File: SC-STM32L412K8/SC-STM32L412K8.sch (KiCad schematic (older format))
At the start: 72 parts, among them J1 usb, J10 PWM, J11 Vibro, J12 +3v, J13 +vibro, J2 +29.6 SiPM, J3 TxD, J4 RxD, J5 SWDIO, J6 SWCLK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

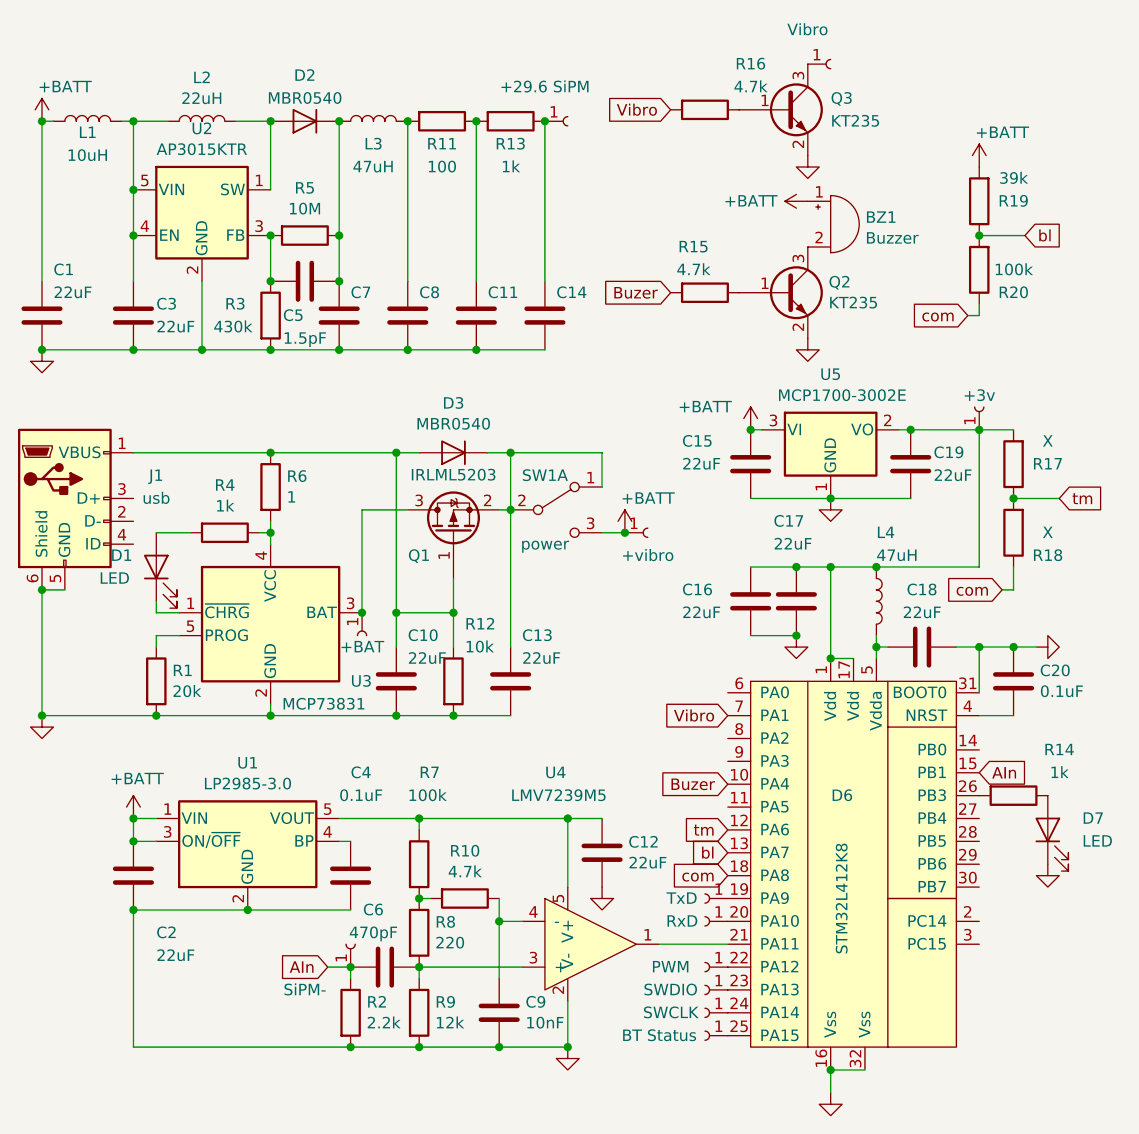
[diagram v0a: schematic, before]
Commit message: изменено:      SC-STM32L412K8/SC-STM32L412K8.kicad_pcb 	изменено:      SC-STM32L412K8/SC-STM32L412K8.kicad_pcb-bak 	изменено:      SC-STM32L412K8/SC-STM32L412K8.net 	изменено:      SC-STM32L412K8/SC-STM32L412K8.sch 	изменено:      SC-STM32L412K8/SC-STM32L412K8.sch-bak 	изменено:      STM32L412K8code/.settings/language.settings.xml
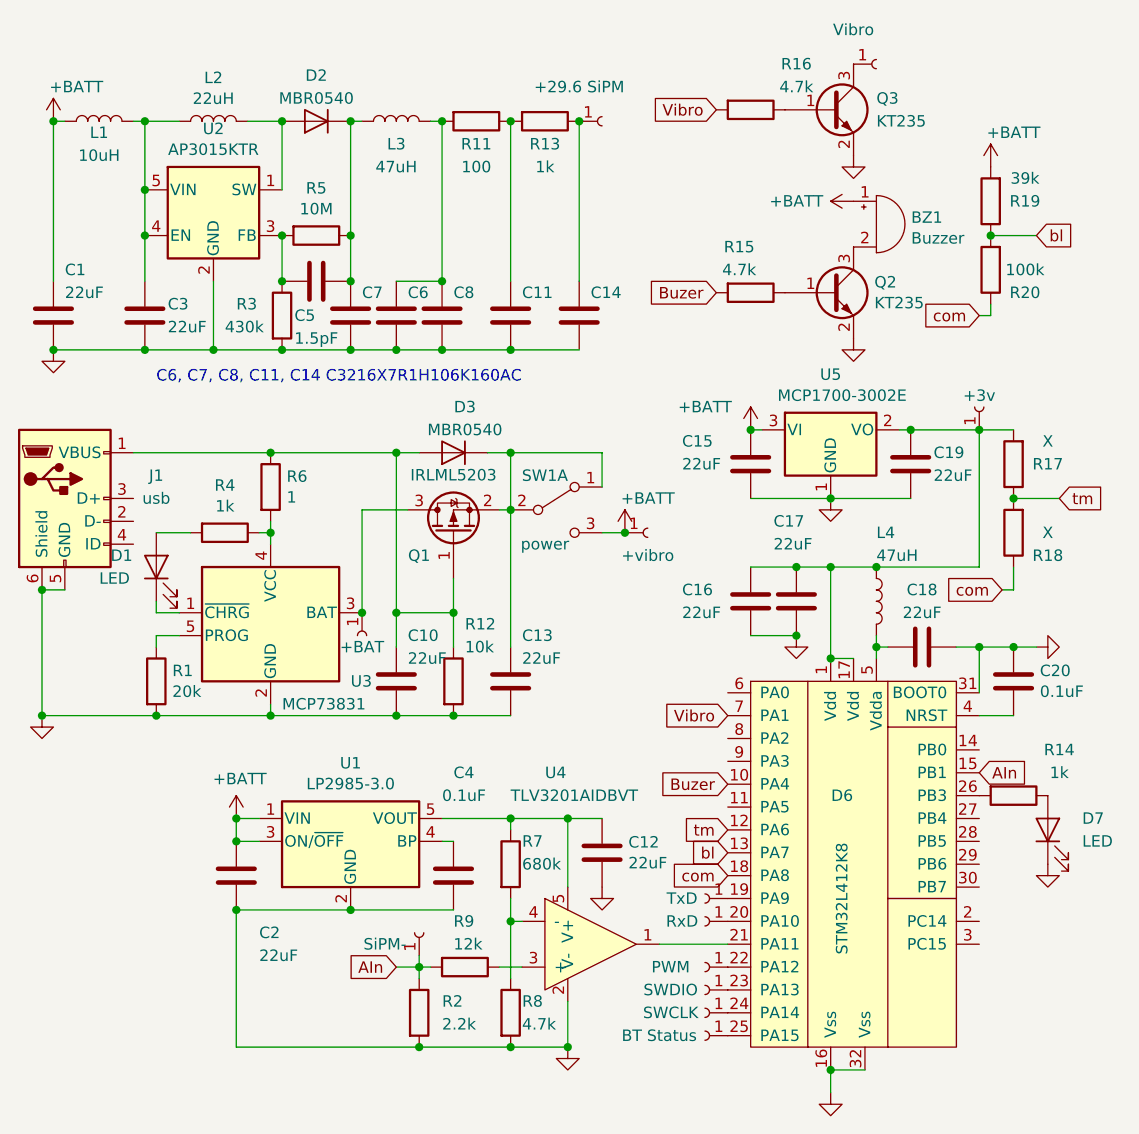
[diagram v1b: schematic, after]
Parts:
- removed C9: 10nF, Capacitor_SMD:C_0603_1608Metric, symbol Device:C
- removed R10: 4.7k, Resistor_SMD:R_0603_1608Metric, symbol Device:R
- C11, C14, C7, C8: value GRM32ER71H106K -> C3216X7R1H106K160AC; footprint Capacitor_SMD:C_1210_3225Metric -> Capacitor_SMD:C_1206_3216Metric
- C6: value 470pF -> C3216X7R1H106K160AC; footprint Capacitor_SMD:C_0603_1608Metric -> Capacitor_SMD:C_1206_3216Metric
- R7: value 100k -> 680k
- R8: value 220 -> 4.7k
- U4: value LMV7239M5 -> TLV3201AIDBVT
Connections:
- net AIn: now also R9.2; no longer C6.2
- net GND: now also C6.1, R8.2; no longer R9.2
- net at R7.2, R8.1: now also U4.4 (-)
- net at R9.1, U4.3 (+): no longer C6.1, R8.2
- net at C8.2, L3.2, R11.2: now also C6.2
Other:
- note added: "C6, C7, C8, C11, C14 C3216X7R1H106K160AC"
- moved on the sheet: BZ1, C1, C11, C14, C2, C3, C4, C5, C7, C8, D2, L1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

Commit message: modified:   AndroidStudio/BLE/app/src/main/java/ru/starline/ble/MainActivity.java 	modified:   SC-STM32L412K8/SC-STM32L412K8.sch 	modified:   SC-STM32L412K8/SC-STM32L412K8.sch-bak 	modified:   SC-STM32L412K8/fp-info-cache
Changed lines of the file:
@@
 	7300 5600 7300 5700
 Connection ~ 7300 5600
-Wire Wire Line
-	7400 3800 7300 3800
 $Comp
 L Device:L L4
@@
 	1    0    0    -1
 $EndComp
-Connection ~ 7300 3800
 Wire Wire Line
 	7950 4050 8100 4050
@@
 Connection ~ 7300 3400
 Wire Wire Line
-	7300 3400 7300 3800
+	7300 3400 7300 3750
 Wire Wire Line
 	7300 3400 7500 3400
@@
 	5250 1450 5200 1450
 Connection ~ 5200 1450
+Wire Wire Line
+	7400 3800 7400 3750
+Wire Wire Line
+	7400 3750 7300 3750
+Connection ~ 7300 3750
+Wire Wire Line
+	7300 3750 7300 3800
 $EndSCHEMATC
